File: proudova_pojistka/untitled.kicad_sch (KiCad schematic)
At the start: 2 parts, among them U1 L78L05_SOT89

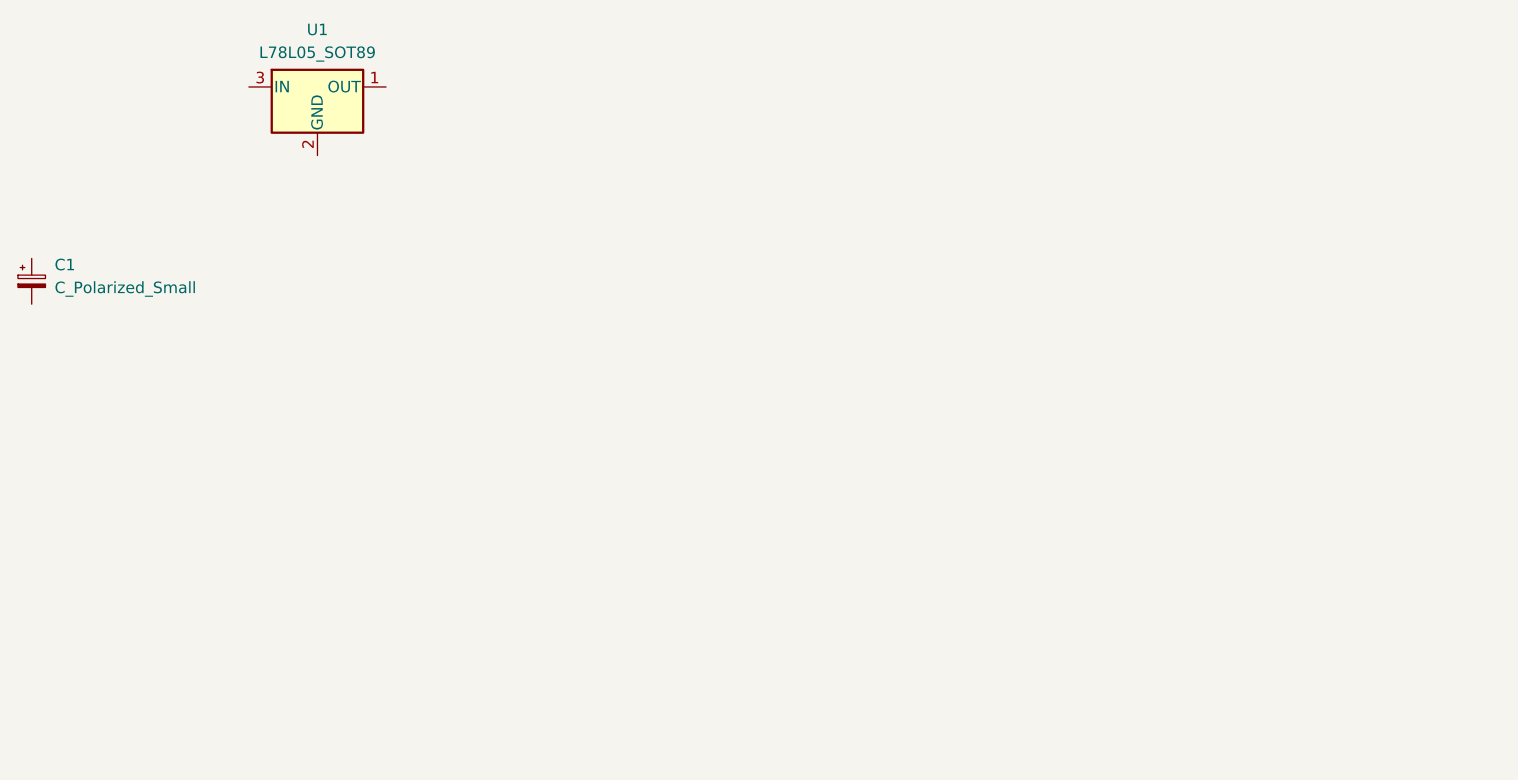
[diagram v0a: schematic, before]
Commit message: Squashed commit of the following:
commit bc8b6beadf69644a5ea80d3999aa0f8eef698db1
Author: stritezsky <stritezskyjirka@seznam.cz>
Date:   Wed Apr 16 21:45:37 2025 +0200

    Ready na konzultaci

commit 592bed4c3ea77b2464c88108ae018bfdb5c68674
Author: stritezsky <stritezskyjirka@seznam.cz>
Date:   Fri Apr 11 21:29:04 2025 +0200

    Schéma + Footprinty

commit 336df2a64e31ad008e1a9e4fa049e0b1b03ab5fe
Author: stritezsky <stritezskyjirka@seznam.cz>
Date:   Tue Apr 8 22:14:07 2025 +0200

    Napájení
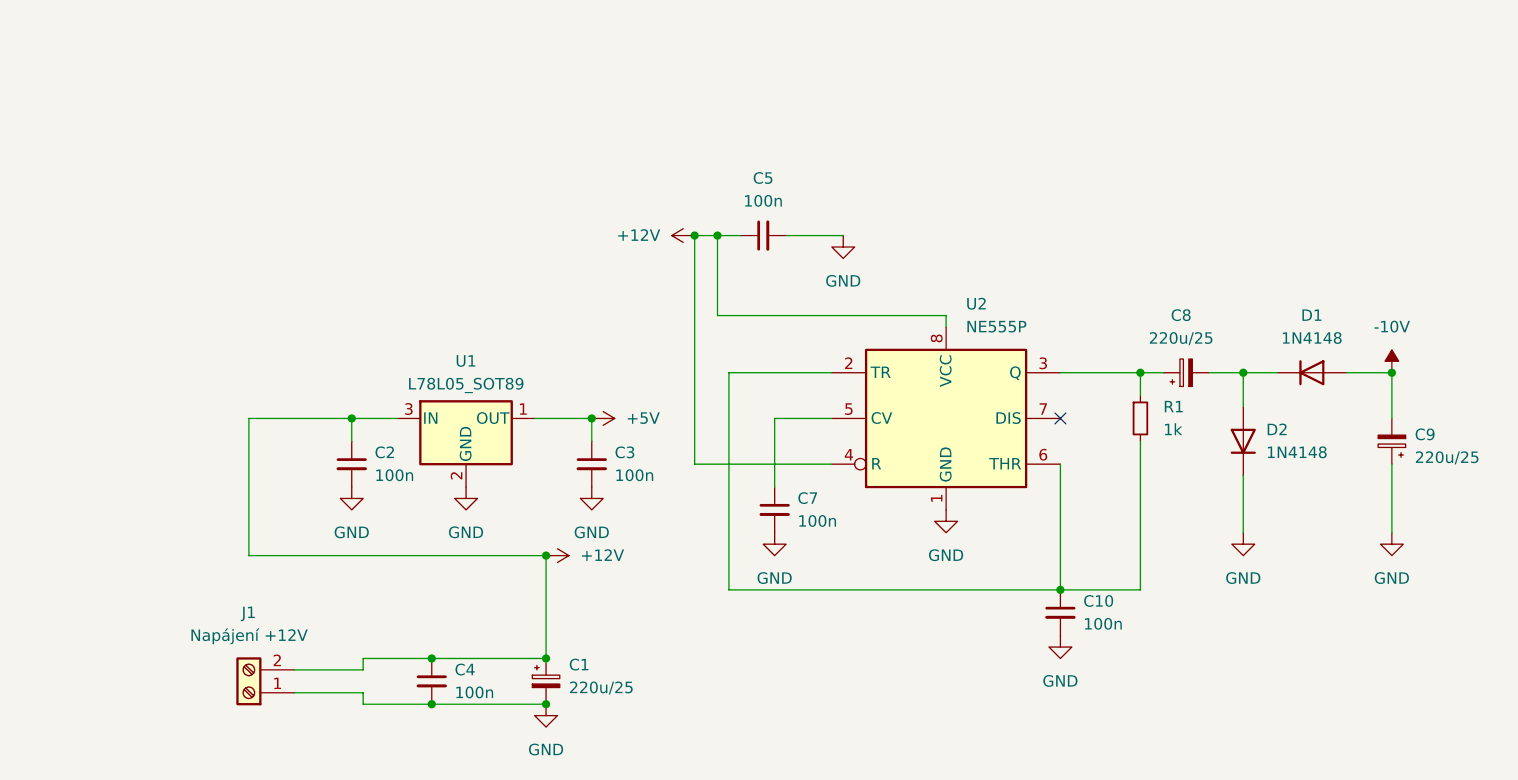
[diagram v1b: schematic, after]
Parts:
- added C10, C2, C3, C4, C5, C7: 100n, Capacitor_THT:C_Disc_D5.0mm_W2.5mm_P5.00mm, symbol Device:C_Small
- added C8, C9: 220u/25, Capacitor_THT:CP_Radial_D8.0mm_P3.50mm, symbol Device:C_Polarized_Small
- added D1, D2: 1N4148, Diode_THT:D_DO-35_SOD27_P7.62mm_Horizontal, symbol Diode:1N4148
- added J1: Napájení +12V, TerminalBlock_Phoenix:TerminalBlock_Phoenix_MKDS-1,5-2-5.08_1x02_P5.08mm_Horizontal, symbol Connector:Screw_Terminal_01x02
- added R1: 1k, Resistor_THT:R_Axial_DIN0918_L18.0mm_D9.0mm_P22.86mm_Horizontal, symbol Device:R_Small
- added U2: NE555P, Package_DIP:DIP-8_W7.62mm, symbol Timer:NE555P
- C1: value C_Polarized_Small -> 220u/25; footprint (none) -> Capacitor_THT:CP_Radial_D8.0mm_P3.50mm
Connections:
- net +5V: now reaches U1.1 (OUT)
- net +5V: now also C3.1
- net GND: now reaches U1.2 (GND)
- net GND: now also C1.2, C10.2, C2.2, C3.2, C4.2, C5.2, C7.2, C9.1, D2.1 (K), J1.1 (Pin_1), U2.1 (GND)
- net +12V: now reaches U1.3 (IN)
- net +12V: now also C1.1, C2.1, C4.1, C5.1, J1.2 (Pin_2), U2.4 (R), U2.8 (VCC)
- new net: C10.1, R1.2, U2.2 (TR), U2.6 (THR)
- new net: C8.1, R1.1, U2.3 (Q)
- new net: C7.1, U2.5 (CV)
- new net: C8.2, D1.1 (K), D2.2 (A)
- new net -10V: C9.2, D1.2 (A)
- no-connect marks 0 -> 1
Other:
- moved on the sheet: C1, U1
